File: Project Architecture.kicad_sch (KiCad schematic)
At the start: 0 parts

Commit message: PCB work
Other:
- removed sheet Section A - Title A
- removed sheet Section B - Title B
- added sheet Connectors (conn.kicad_sch)
- added sheet Drivers (drivers.kicad_sch)
- added sheet MCU (mcu.kicad_sch)
- added sheet Power (power.kicad_sch)
- note removed: "Page 4"
- note removed: "Page 5"

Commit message: PCB schematic design
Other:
- sheet Connectors ports: added IMU_SCL, IMU_SDA, USB_D+, USB_D-; removed none
- sheet Drivers ports: added {MOTOR2}, {MOTOR3}, {TMC2}, {TMC3}; removed none
- sheet Power ports: added INA_SCL, INA_SDA; removed none
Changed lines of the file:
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@@
 	)
 	(sheet
-		(at 143.51 60.96)
-		(size 33.655 20.955)
+		(at 167.64 59.69)
+		(size 12.7 25.4)
 		(exclude_from_sim no)
 		(in_bom yes)
@@
 		)
 		(property "Sheetname" "Drivers"
-			(at 143.51 60.2484 0)
+			(at 167.64 58.9784 0)
 			(show_name no)
 			(do_not_autoplace no)
@@
 		)
 		(property "Sheetfile" "drivers.kicad_sch"
-			(at 143.51 82.4996 0)
+			(at 167.64 85.6746 0)
+			(hide yes)
 			(show_name no)
 			(do_not_autoplace no)
@@
 		)
 		(pin "{A4988}" input
-			(at 177.165 63.5 0)
+			(at 180.34 82.55 0)
 			(effects
 				(font
@@
 		)
 		(pin "{MOTOR1}" input
-			(at 177.165 67.31 0)
+			(at 180.34 66.04 0)
 			(effects
 				(font
@@
 		)
 		(pin "{TMC1}" input
-			(at 177.165 71.12 0)
+			(at 180.34 63.5 0)
+			(effects
+				(font
+					(size 1.27 1.27)
+				)
+				(justify right)
+			)
+		)
+		(pin "{MOTOR2}" input
+			(at 180.34 72.39 0)
+			(effects
+				(font
+					(size 1.27 1.27)
+				)
+				(justify right)
+			)
+		)
+		(pin "{MOTOR3}" input
+			(at 180.34 78.74 0)
+			(effects
+				(font
+					(size 1.27 1.27)
+				)
+				(justify right)
+			)
+		)
+		(pin "{TMC2}" input
+			(at 180.34 69.85 0)
+			(effects
+				(font
+					(size 1.27 1.27)
+				)
+				(justify right)
+			)
+		)
+		(pin "{TMC3}" input
+			(at 180.34 76.2 0)
 			(effects
 				(font
@@
 	)
 	(sheet
-		(at 190.5 90.805)
-		(size 19.05 14.605)
+		(at 226.06 77.47)
+		(size 15.24 7.62)
 		(exclude_from_sim no)
 		(in_bom yes)
@@
 		)
 		(property "Sheetname" "Power"
-			(at 190.5 90.0934 0)
+			(at 226.06 76.7584 0)
 			(show_name no)
 			(do_not_autoplace no)
@@
 		)
 		(property "Sheetfile" "power.kicad_sch"
-			(at 190.5 105.9946 0)
-			(show_name no)
-			(do_not_autoplace no)
-			(effects
-				(font
-					(size 1.27 1.27)
-				)
-				(justify left top)
+			(at 226.06 85.6746 0)
+			(hide yes)
+			(show_name no)
+			(do_not_autoplace no)
+			(effects
+				(font
+					(size 1.27 1.27)
+				)
+				(justify left top)
+			)
+		)
+		(pin "INA_SCL" input
+			(at 226.06 82.55 180)
+			(effects
+				(font
+					(size 1.27 1.27)
+				)
+				(justify left)
+			)
+		)
+		(pin "INA_SDA" input
+			(at 226.06 80.01 180)
+			(effects
+				(font
+					(size 1.27 1.27)
+				)
+				(justify left)
 			)
 		)
@@
 	)
 	(sheet
-		(at 190.5 60.96)
-		(size 38.1 20.955)
+		(at 184.15 59.69)
+		(size 38.1 25.4)
 		(exclude_from_sim no)
 		(in_bom yes)
@@
 		)
 		(property "Sheetname" "MCU"
-			(at 190.5 60.2484 0)
+			(at 184.15 58.9784 0)
 			(show_name no)
 			(do_not_autoplace no)
@@
 		)
 		(property "Sheetfile" "mcu.kicad_sch"
-			(at 190.5 82.4996 0)
+			(at 184.15 85.6746 0)
+			(hide yes)
 			(show_name no)
 			(do_not_autoplace no)
@@
 	)
 	(sheet
-		(at 222.25 100.33)
-		(size 17.78 13.97)
+		(at 226.06 59.69)
+		(size 12.7 15.24)
 		(exclude_from_sim no)
 		(in_bom yes)
@@
 		)
 		(property "Sheetname" "Connectors"
-			(at 222.25 99.6184 0)
+			(at 226.06 58.9784 0)
 			(show_name no)
 			(do_not_autoplace no)
@@
 		)
 		(property "Sheetfile" "conn.kicad_sch"
-			(at 222.25 114.8846 0)
-			(show_name no)
-			(do_not_autoplace no)
-			(effects
-				(font
-					(size 1.27 1.27)
-				)
-				(justify left top)
-			)
-		)
+			(at 226.06 75.5146 0)
+			(hide yes)
+			(show_name no)
+			(do_not_autoplace no)
+			(effects
+				(font
+					(size 1.27 1.27)
+				)
+				(justify left top)
+			)
+		)
+		(pin "IMU_SCL" input
+			(at 226.06 62.865 180)
+			(effects
+				(font
+					(size 1.27 1.27)
+				)
+				(justify left)
+			)
+		)
+		(pin "IMU_SDA" input
+			(at 226.06 65.405 180)
+			(effects
+				(font
+					(size 1.27 1.27)
+				)
+				(justify left)
+			)
+		)
+		(pin "USB_D+" input
+			(at 226.06 67.945 180)
+			(effects
+				(font
+					(size 1.27 1.27)
+				)
+				(justify left)
+			)
+		)
+		(pin "USB_D-" input
+			(at 226.06 70.485 180)
+			(effects
+				(font
+					(size 1.27 1.27)
+				)
+				(justify left)
+			)
+		)

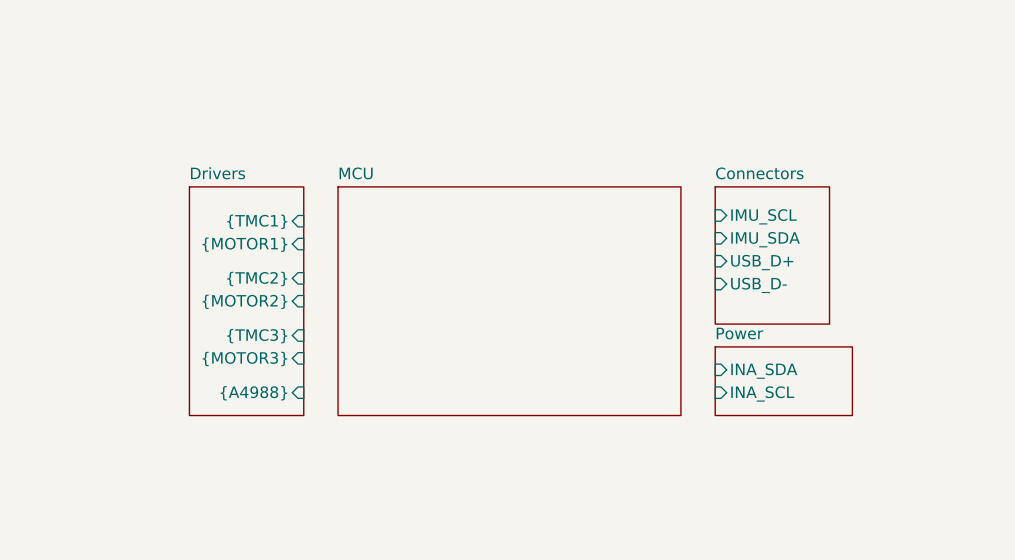
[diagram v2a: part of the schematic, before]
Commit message: Connected hierarchical boards
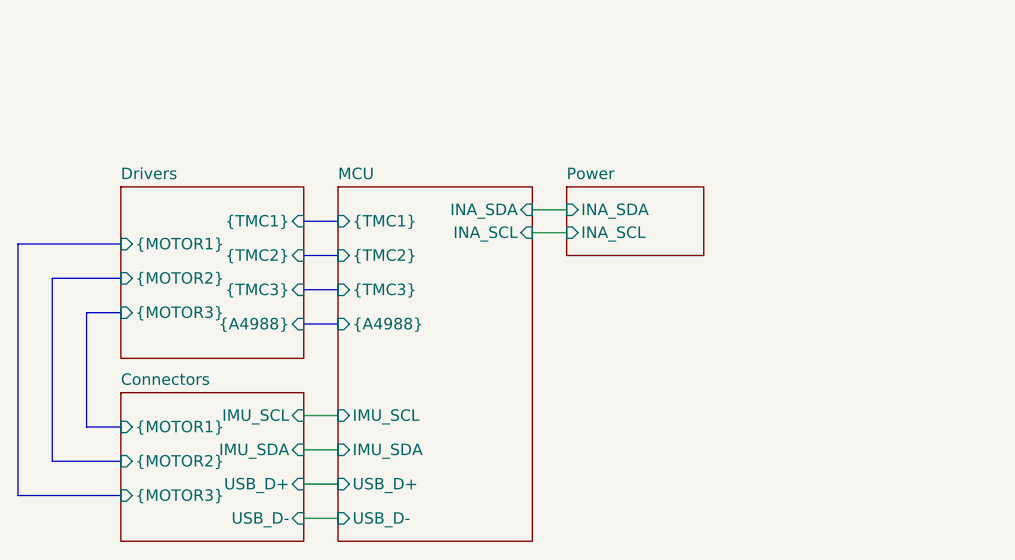
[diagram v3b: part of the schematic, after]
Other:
- sheet Connectors ports: added {MOTOR1}, {MOTOR2}, {MOTOR3}; removed none
- sheet MCU ports: added IMU_SCL, IMU_SDA, INA_SCL, INA_SDA, USB_D+, USB_D-, {A4988}, {TMC1}, {TMC2}, {TMC3}; removed none
